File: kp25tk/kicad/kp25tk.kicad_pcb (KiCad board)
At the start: 2 copper layers, 100 x 137.4 mm, 107 parts, among them J1 Host Connector, J2 Config Header, J3 Power In, J4 Row Select In, J5 Column Out, J6 NMI Out, J7 Reset Out, J8 Switch, SW0 KEY00, SW1 KEY01, SW10 KEY0A, SW11 KEY0B, SW12 KEY0C, SW13 KEY0D, SW14 KEY0E, SW15 KEY0F, SW16 KEY10, SW17 KEY11, SW18 KEY12, SW19 KEY13, SW2 KEY02, SW20 KEY14, SW21 KEY15, SW22 KEY16, SW23 KEY17, SW24 NMI, SW25 RESET, SW27 SWITCH, SW3 KEY03, SW4 KEY04, SW5 KEY05, SW6 KEY06, SW7 KEY07, SW8 KEY08, SW9 KEY09, U1 74HLS14

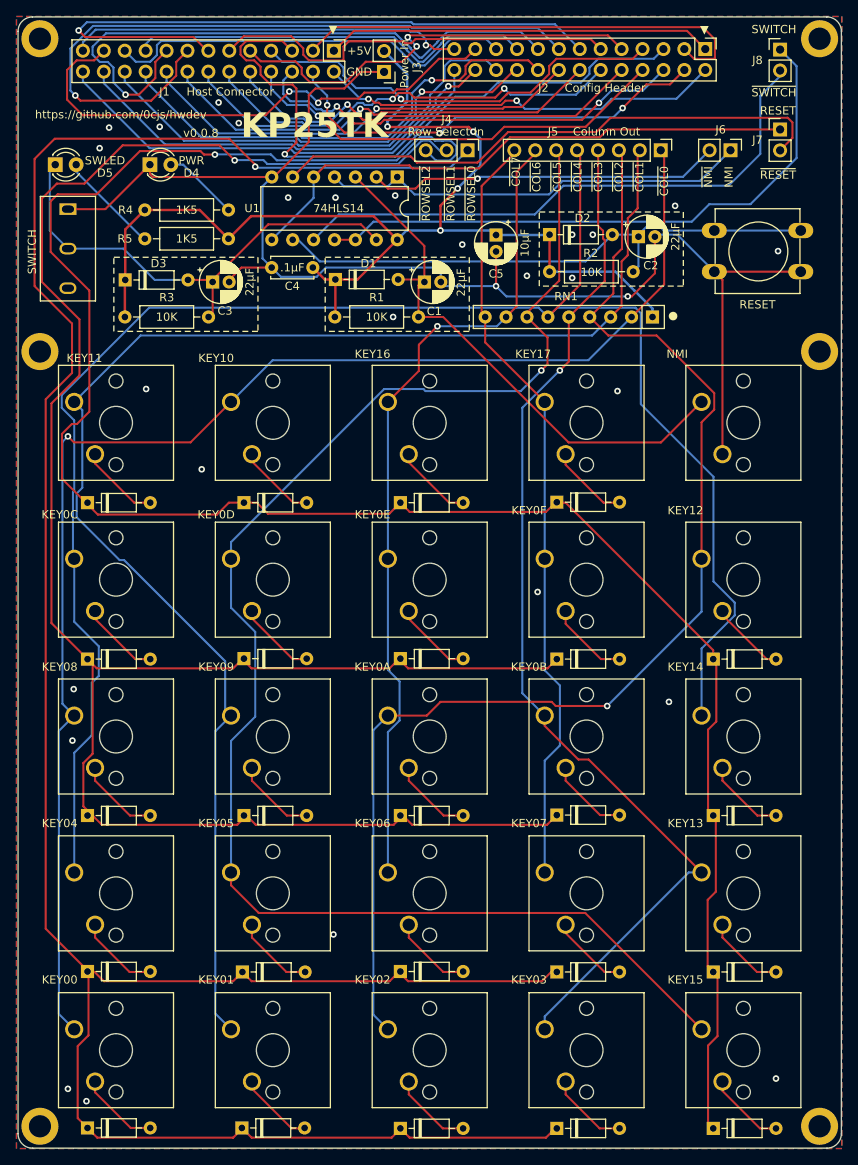
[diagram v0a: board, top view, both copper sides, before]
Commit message: TEST kp25tk pcb: Move bottom edge cut up to get <100×100 board
This is intended to get a cheap prototype from JLCPCB; we still get
three rows of keys which is enough to test with.

All the stuff outside the edge cut is still left there; we'll see if
JLCPCB just ignores that or if we have to remove that too.
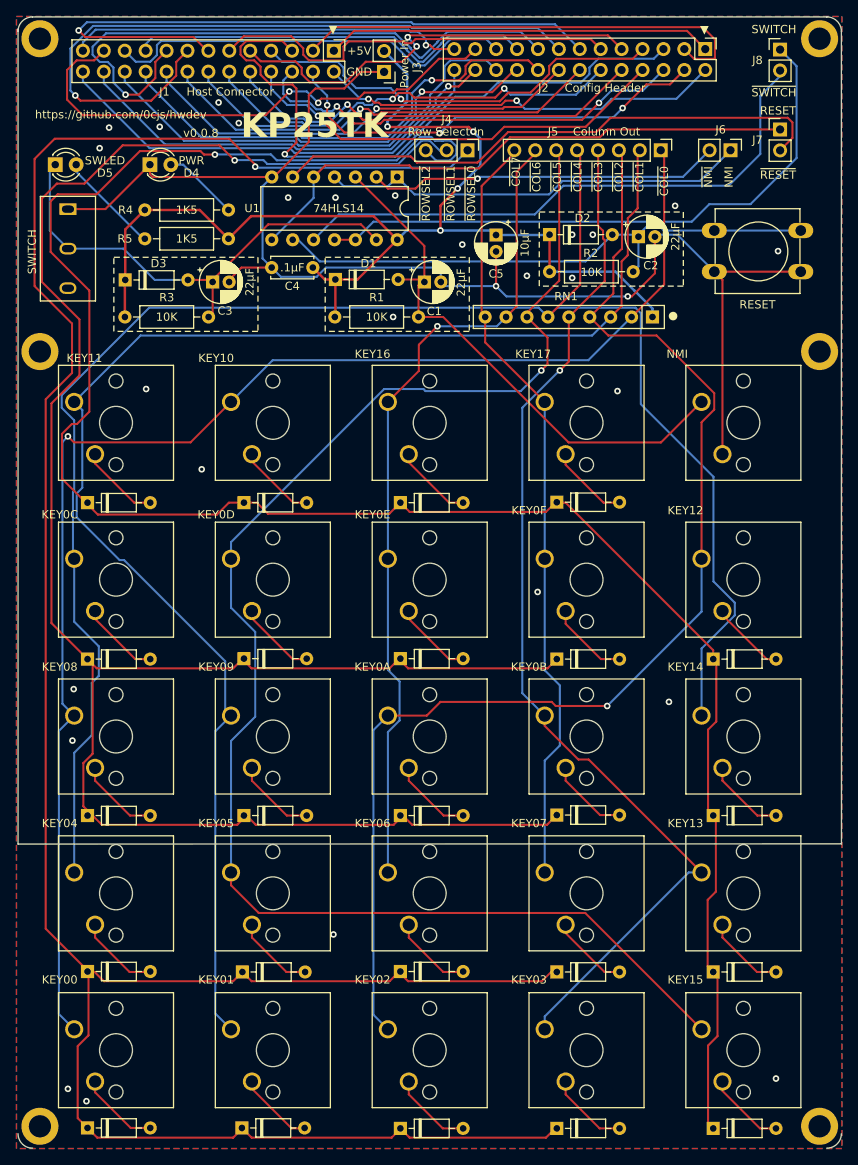
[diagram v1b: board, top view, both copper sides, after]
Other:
- outline, holes or cut-outs redrawn
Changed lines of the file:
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@@
 	(gr_line
 		(start 144.725 47.3)
-		(end 144.725 181.2)
+		(end 144.739216 145.995244)
 		(stroke
 			(width 0.1)
-			(type default)
+			(type solid)
 		)
 		(layer "Edge.Cuts")
@@
 	)
 	(gr_line
-		(start 142.965 182.955)
-		(end 46.485 182.955)
+		(start 144.739216 145.995244)
+		(end 44.725 146.02)
 		(stroke
 			(width 0.1)
@@
 	)
 	(gr_line
-		(start 44.725 181.2)
-		(end 44.725 47.31)
+		(start 44.725 146.02)
+		(end 44.725 47.02)
 		(stroke
 			(width 0.1)
-			(type default)
+			(type solid)
 		)
 		(layer "Edge.Cuts")

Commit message: kp25tk pcb: Remove all stuff below the bottom cut edge
Turns out that, though in the Gerber viewer on JLCPCB we seemed to be
getting what we wanted, it bases the board size not on the edge cuts
but on everything that's on the board, so though the Gerber output
showed an ~100×100 board, we were being charged for a 100×130 or
whatever it was.

This gets the board price down, but unfortunately it still seems too
big for $1 OCS NEP shipping, causing us to have to use the $10 shipping
instead. So we need to look at whether we can cut this down further.
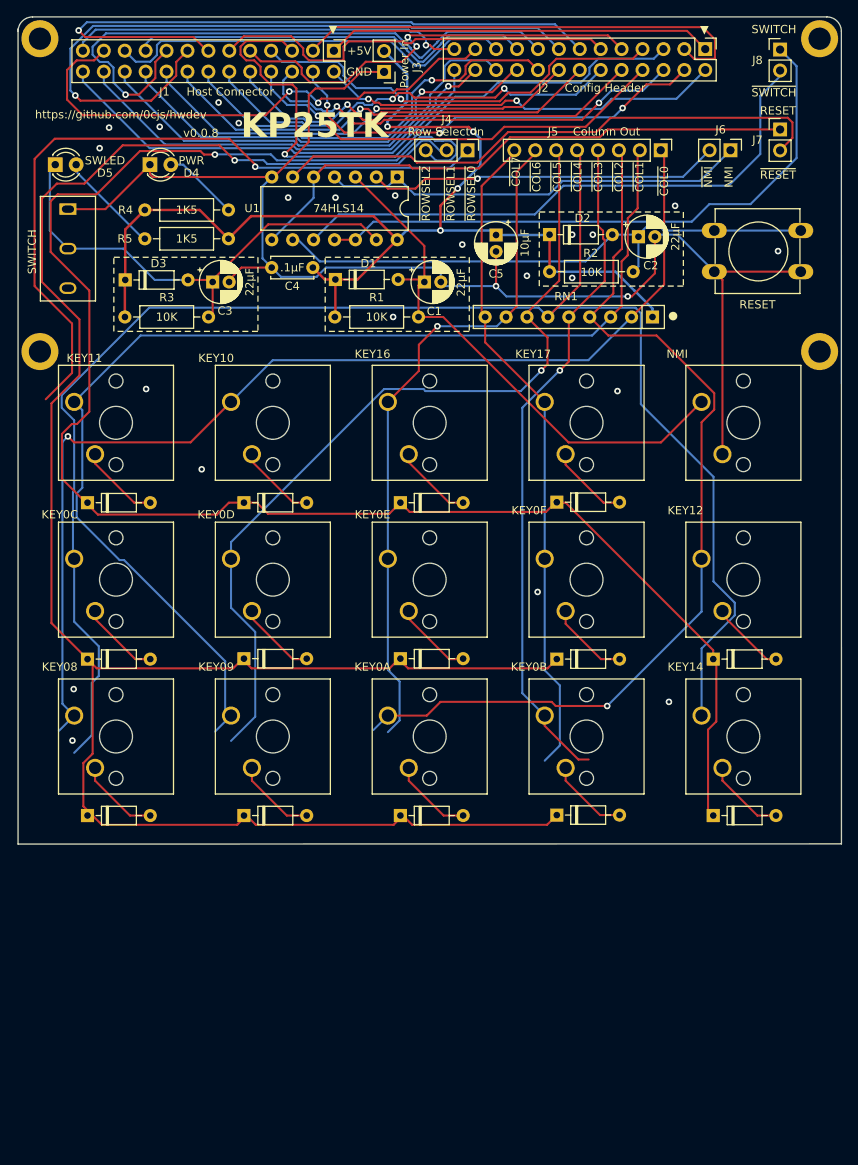
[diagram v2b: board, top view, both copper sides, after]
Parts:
- removed the ? at (47.4, 180.3)
- removed the ? at (142.1, 180.3)
- removed D10, D11, D12, D13, D14, D15, D27, D29, D8, D9: 1N5819, Diode_THT:D_DO-35_SOD27_P7.62mm_Horizontal
- removed SW0: KEY00, Button_Switch_Keyboard:SW_Cherry_MX_1.00u_PCB
- removed SW1: KEY01, Button_Switch_Keyboard:SW_Cherry_MX_1.00u_PCB
- removed SW19: KEY13, Button_Switch_Keyboard:SW_Cherry_MX_1.00u_PCB
- removed SW2: KEY02, Button_Switch_Keyboard:SW_Cherry_MX_1.00u_PCB
- removed SW21: KEY15, Button_Switch_Keyboard:SW_Cherry_MX_1.00u_PCB
- removed SW3: KEY03, Button_Switch_Keyboard:SW_Cherry_MX_1.00u_PCB
- removed SW4: KEY04, Button_Switch_Keyboard:SW_Cherry_MX_1.00u_PCB
- removed SW5: KEY05, Button_Switch_Keyboard:SW_Cherry_MX_1.00u_PCB
- removed SW6: KEY06, Button_Switch_Keyboard:SW_Cherry_MX_1.00u_PCB
- removed SW7: KEY07, Button_Switch_Keyboard:SW_Cherry_MX_1.00u_PCB
- removed SWKC0, SWKC1, SWKC19, SWKC2, SWKC21, SWKC3, SWKC4, SWKC5, SWKC6, SWKC7: Keycap, Button_Switch_Keyboard_Keycap:SW_Cherry_MX_Keycap_1.00u
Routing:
- net Net-(D10-K): track 299.2 -> 88.5 mm
- net Net-(J5-~{COL5}): track 184.9 -> 103.0 mm
- net Net-(J5-~{COL3}): track 129.8 -> 82.6 mm
- net Net-(D24-K): track 248.4 -> 209.2 mm
- net Net-(J5-~{COL2}): track 151.5 -> 114.4 mm
- net Net-(J5-~{COL0}): track 171.6 -> 134.5 mm
- net Net-(J5-~{COL1}): track 177.7 -> 140.7 mm
- net Net-(J5-~{COL6}): track 100.7 -> 83.7 mm
- net Net-(J5-~{COL4}): track 214.3 -> 199.8 mm
- net Net-(J5-~{COL7}): track 94.2 -> 80.6 mm
- net Net-(D27-A): track 10.1 -> 0.00 mm
- net Net-(D8-A): track 9.80 -> 0.00 mm
- net Net-(D12-A): track 9.80 -> 0.00 mm
- net Net-(D13-A): track 9.75 -> 0.00 mm
- net Net-(D14-A): track 9.70 -> 0.00 mm
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- removed copper zone on B.Cu, net Earth
- removed copper zone on F.Cu, net Earth
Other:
- board size 100 x 137.4 mm -> 100 x 100.5 mm

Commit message: TESTING kp25tk pcb: More tweaking to get down to < 99×99
JLCPCB reads as 98.77 × 98.25 mm. And this does work for OCS NEP $1 shipping.
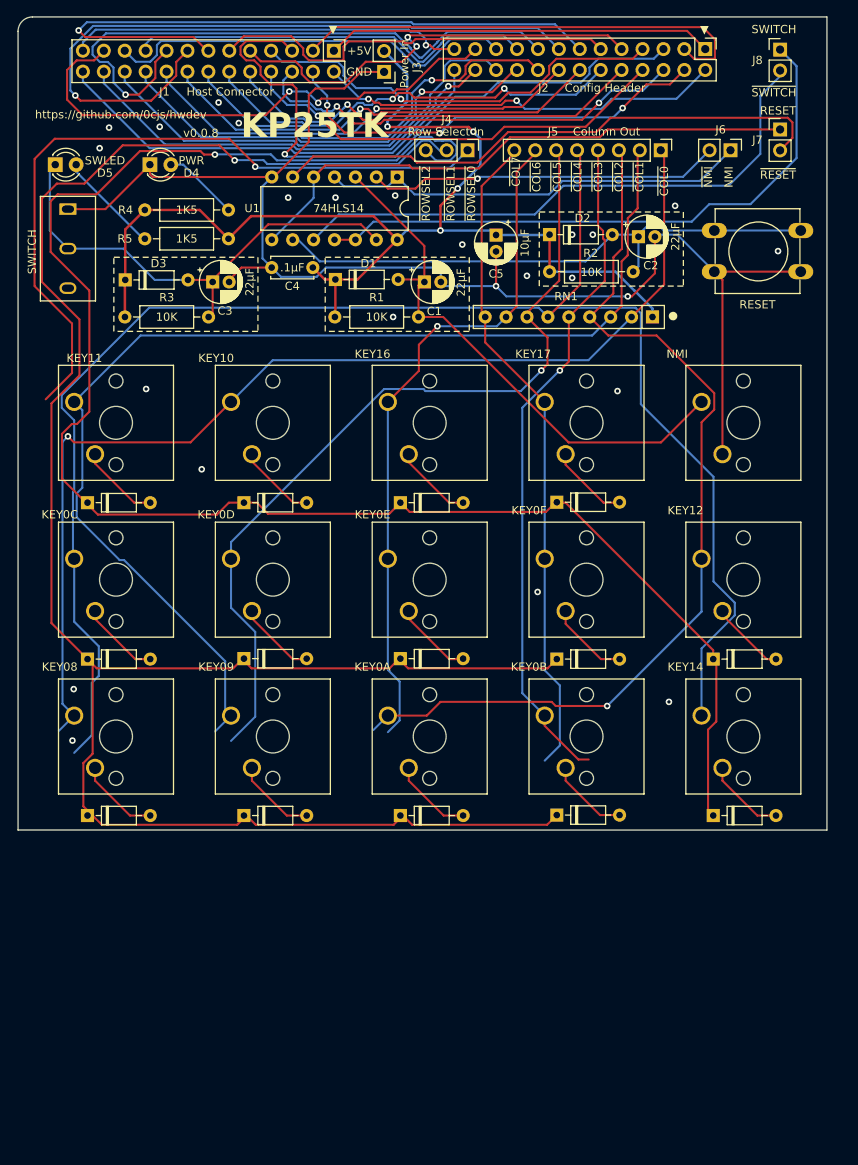
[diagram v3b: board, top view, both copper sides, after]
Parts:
- removed ? (x4): , 
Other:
- board size 100 x 100.5 mm -> 98.2 x 98.8 mm
